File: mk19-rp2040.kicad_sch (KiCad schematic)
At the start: 145 parts, among them J1 USB_C_Receptacle_USB2.0, J10 Conn_01x02, J11 Conn_01x03_Socket, J12 USB_C_Receptacle_USB2.0, J13 USB_C_Receptacle_USB2.0, J2 Conn_01x03_Socket, J3 Conn_01x02_Socket, J4 Conn_01x06_Socket, J5 Conn_01x02, J7 Conn_01x02_Socket, J8 Conn_01x02_Socket, J9 Conn_01x02_Socket, T1 Conn_01x01_Socket, T10 Conn_01x01_Socket, T11 Conn_01x01_Socket, T12 Conn_01x01_Socket, T13 Conn_01x01_Socket, T14 Conn_01x01_Socket, T15 Conn_01x01_Socket, T2 Conn_01x01_Socket, T3 Conn_01x01_Socket, T5 Conn_01x01_Socket, T6 Conn_01x01_Socket, T7 Conn_01x01_Socket, T9 Conn_01x01_Socket, U1 RP2040, U10 1N4148W_C81598, U11 1N4148W_C81598, U12 1N4148W_C81598, U13 1N4148W_C81598, U14 1N4148W_C81598, U15 1N4148W_C81598, U16 W25Q128JVSIQTR, U3 XC6210B332MR-G, U6 8_01A0_008200, U7 8_01A0_008200, U9 1N4148W_C81598, Y1 Crystal_GND24

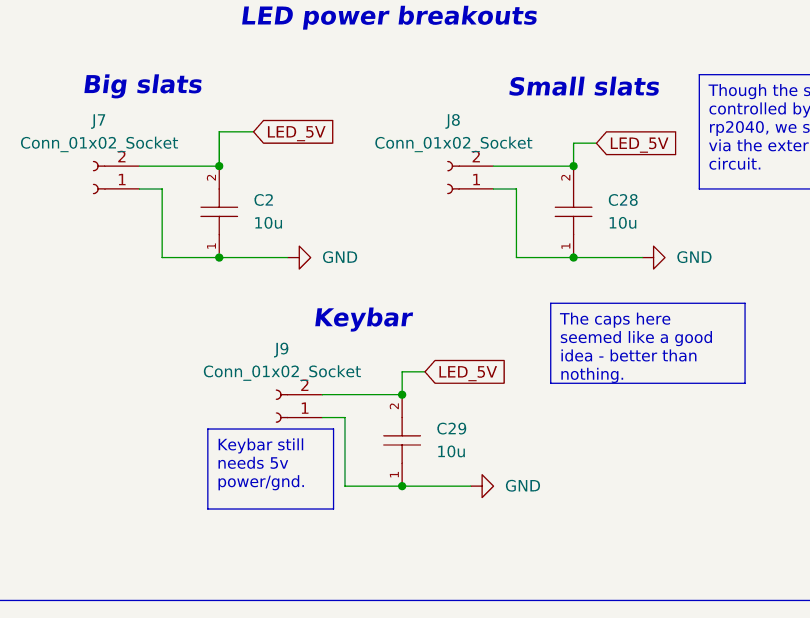
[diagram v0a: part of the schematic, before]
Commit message: removing the other 10u caps and relocating the power in plug
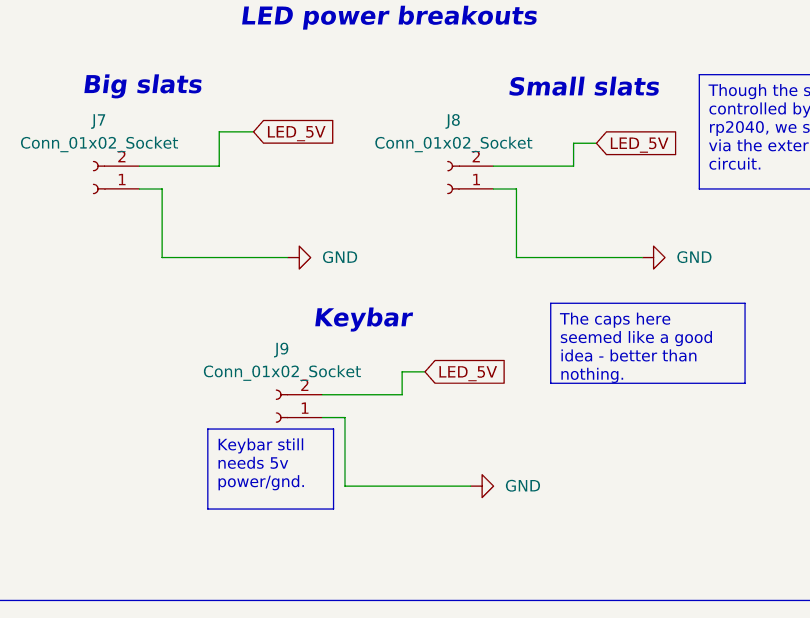
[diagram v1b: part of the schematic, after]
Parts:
- removed C2, C28, C29: 10u, ct-kicad:C0805, symbol ct-kicad:GRM21BR61H106KE43L

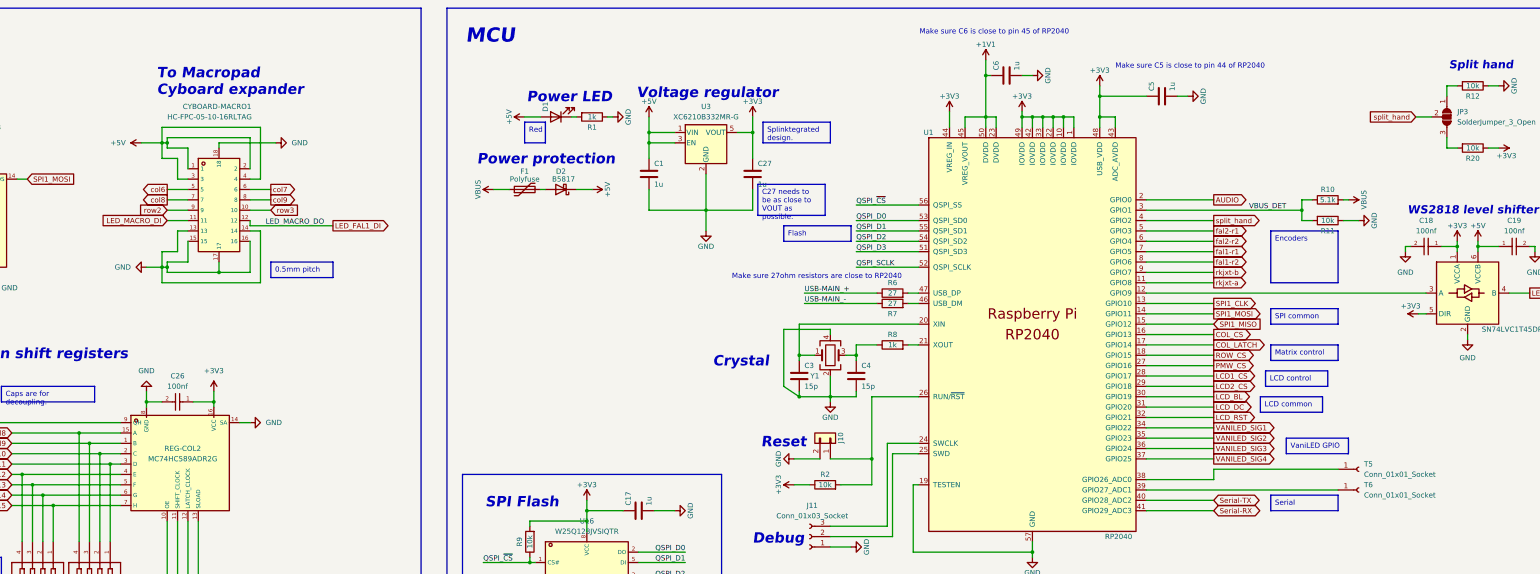
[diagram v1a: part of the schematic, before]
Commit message: replaced the macro connector with a more solid-looking part, more rework
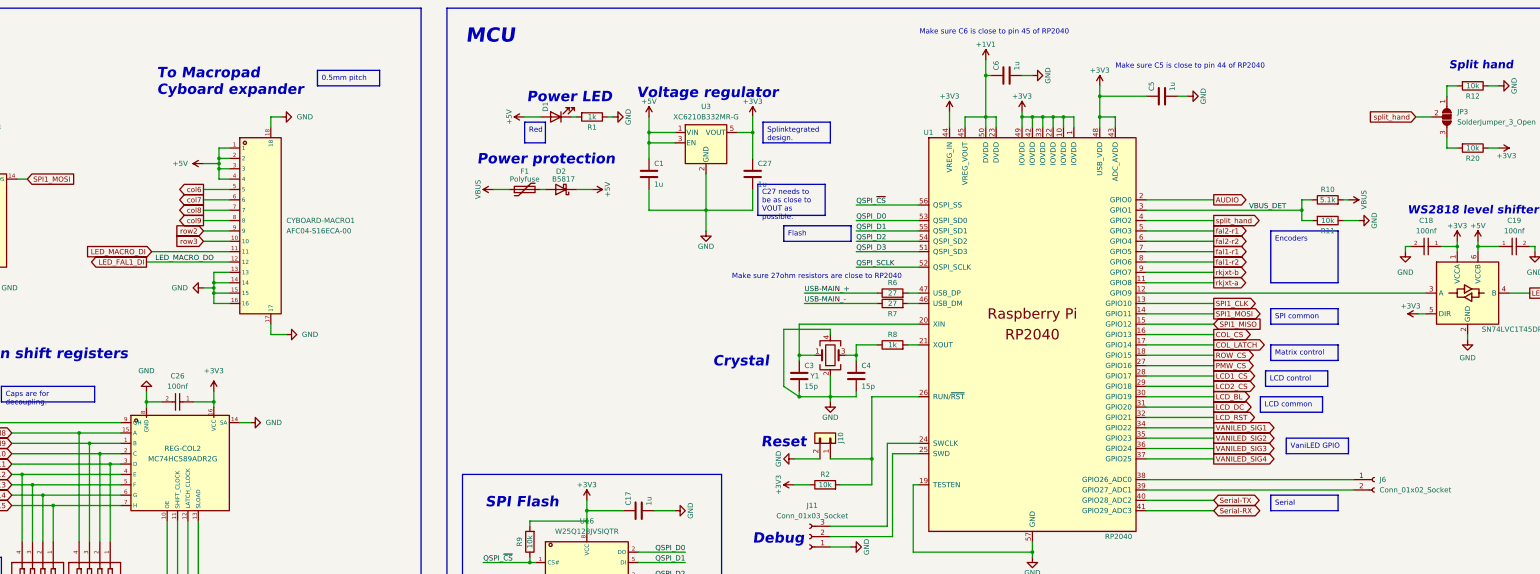
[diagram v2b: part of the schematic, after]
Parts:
- removed CYBOARD-MACRO1: HC-FPC-05-10-16RLTAG, ct-kicad:FPC-SMD_16P-P0.50_HCTL_HC-FPC-05-10-16RLTAG, symbol ct-kicad:0_5K-A-16PBF
- removed T5, T6: Conn_01x01_Socket, Connector_Pin:Pin_D1.0mm_L10.0mm, symbol Connector:Conn_01x01_Socket
- added CYBOARD-MACRO1: AFC04-S16ECA-00, ct-kicad:FPC-SMD_AFC04-S16ECA-00, symbol ct-kicad:AFC04-S16ECA-00
- added J6: Conn_01x02_Socket, Connector_JST:JST_XH_S2B-XH-A_1x02_P2.50mm_Horizontal, symbol Connector:Conn_01x02_Socket
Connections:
- net +5V: now also CYBOARD-MACRO1.1, CYBOARD-MACRO1.2, CYBOARD-MACRO1.3, CYBOARD-MACRO1.4
- net GND: now also CYBOARD-MACRO1.13, CYBOARD-MACRO1.14, CYBOARD-MACRO1.15, CYBOARD-MACRO1.16, CYBOARD-MACRO1.17, CYBOARD-MACRO1.18
- net LED_FAL1_DI: now also CYBOARD-MACRO1.12
- net LED_MACRO_DI: now also CYBOARD-MACRO1.11
- net col6: now also CYBOARD-MACRO1.5
- net col7: now also CYBOARD-MACRO1.6
- net col8: now also CYBOARD-MACRO1.7
- net col9: now also CYBOARD-MACRO1.8
- net row2: now also CYBOARD-MACRO1.9
- net row3: now also CYBOARD-MACRO1.10
- net at U1.38 (GPIO26_ADC0): now also J6.1 (Pin_1)
- net at U1.39 (GPIO27_ADC1): now also J6.2 (Pin_2)

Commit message: fixing silkscreen, changing out polyfuses to larger, improving trace routing
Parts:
- removed F1: Polyfuse, Fuse:Fuse_0603_1608Metric, symbol Device:Polyfuse
- added F1: Polyfuse, ct-kicad:F1206, symbol ct-kicad:RF1989-000
- F2: footprint Fuse:Fuse_0603_1608Metric -> ct-kicad:F1206; symbol Device:Polyfuse -> ct-kicad:RF1989-000; LCSC C69679 -> C2892425
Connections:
- net +5V: no longer VANILED1.2 (Pin_2)
- net VBUS: now also F1.1
- net at JP1.2 (C), JP4.2 (C): now also VANILED1.2 (Pin_2)
- net at D2.2 (A): now also F1.2
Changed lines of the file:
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@@
 	)
 	(junction
+		(at 152.4 414.02)
+		(diameter 0)
+		(color 0 0 0 0)
+	)
+	(junction
 		(at 168.91 129.54)
 		(diameter 0)
@@
 	(wire
 		(pts
-			(xy 339.09 62.23) (xy 340.36 62.23)
-		)
-		(stroke
-			(width 0)
-			(type default)
-		)
-	)
-	(wire
-		(pts
 			(xy 571.5 52.07) (xy 574.04 52.07)
 		)
@@
 	(wire
 		(pts
+			(xy 152.4 414.02) (xy 152.4 425.45)
+		)
+		(stroke
+			(width 0)
+			(type default)
+		)
+	)
+	(wire
+		(pts
 			(xy 143.51 129.54) (xy 168.91 129.54)
 		)
@@
 	(wire
 		(pts
-			(xy 173.99 419.1) (xy 175.26 419.1)
-		)
-		(stroke
-			(width 0)
-			(type default)
-		)
-	)
-	(wire
-		(pts
 			(xy 233.68 265.43) (xy 243.84 265.43)
 		)
@@
 	(wire
 		(pts
-			(xy 152.4 412.75) (xy 152.4 425.45)
+			(xy 152.4 412.75) (xy 152.4 414.02)
 		)
 		(stroke
@@
 	(wire
 		(pts
-			(xy 171.45 375.92) (xy 175.26 375.92)
+			(xy 171.45 375.92) (xy 189.23 375.92)
 		)
 		(stroke
@@
 	(wire
 		(pts
+			(xy 189.23 375.92) (xy 189.23 414.02)
+		)
+		(stroke
+			(width 0)
+			(type default)
+		)
+	)
+	(wire
+		(pts
 			(xy 487.68 138.43) (xy 504.19 138.43)
 		)
@@
 	(wire
 		(pts
+			(xy 173.99 419.1) (xy 175.26 419.1)
+		)
+		(stroke
+			(width 0)
+			(type default)
+		)
+	)
+	(wire
+		(pts
 			(xy 217.17 137.16) (xy 236.22 137.16)
 		)
@@
 	(wire
 		(pts
-			(xy 160.02 419.1) (xy 166.37 419.1)
+			(xy 160.02 419.1) (xy 163.83 419.1)
 		)
 		(stroke
@@
 	(wire
 		(pts
+			(xy 327.66 62.23) (xy 328.93 62.23)
+		)
+		(stroke
+			(width 0)
+			(type default)
+		)
+	)
+	(wire
+		(pts
 			(xy 222.25 275.59) (xy 231.14 275.59)
 		)
@@
 	(wire
 		(pts
+			(xy 339.09 62.23) (xy 340.36 62.23)
+		)
+		(stroke
+			(width 0)
+			(type default)
+		)
+	)
+	(wire
+		(pts
 			(xy 487.68 110.49) (xy 504.19 110.49)
 		)
@@
 	(wire
 		(pts
+			(xy 189.23 414.02) (xy 152.4 414.02)
+		)
+		(stroke
+			(width 0)
+			(type default)
+		)
+	)
+	(wire
+		(pts
 			(xy 335.28 44.45) (xy 339.09 44.45)
 		)
@@
 	(wire
 		(pts
-			(xy 327.66 62.23) (xy 331.47 62.23)
-		)
-		(stroke
-			(width 0)
-			(type default)
-		)
-	)
-	(wire
-		(pts
 			(xy 535.94 69.85) (xy 539.75 69.85)
 		)
@@
 	)
 	(symbol
-		(lib_id "Device:Polyfuse")
-		(at 335.28 62.23 90)
+		(lib_id "Device:FerriteBead_Small")
+		(at 368.3 322.58 270)
 		(unit 1)
 		(exclude_from_sim no)
@@
 		(on_board yes)
 		(dnp no)
-		(property "Reference" "F1"
-			(at 335.28 57.785 90)
+		(property "Reference" "FB2"
+			(at 363.22 325.12 90)
 			(effects
 				(font
 					(size 1.27 1.27)
 				)
+				(justify left)
 			)
 		)
-		(property "Value" "Polyfuse"
-			(at 335.28 59.69 90)
+		(property "Value" "FerriteBead_Small"
+			(at 367.0682 325.12 0)
 			(effects
 				(font
 					(size 1.27 1.27)
 				)
+				(justify left)
+				(hide yes)
 			)
 		)
-		(property "Footprint" "Fuse:Fuse_0603_1608Metric"
-			(at 340.36 60.96 0)
+		(property "Footprint" "Inductor_SMD:L_0603_1608Metric"
+			(at 368.3 320.802 90)
 			(effects
 				(font
 					(size 1.27 1.27)
 				)
-				(justify left)
 				(hide yes)
 			)
 		)
 		(property "Datasheet" "~"
-			(at 335.28 62.23 0)
+			(at 368.3 322.58 0)
 			(effects
 				(font
@@
 		)
 		(property "Description" ""
-			(at 335.28 62.23 0)
+			(at 368.3 322.58 0)
 			(effects
 				(font
@@
 			)
 		)
-		(property "LCSC" "C69679"
-			(at 335.28 62.23 0)
+		(property "LCSC" "C98288"
+			(at 368.3 322.58 0)
 			(effects
 				(font
@@
 			(project "mk19-rp2040"
 				(path "/7353e96a-343a-4876-b497-b1d205a14d97"
-					(reference "F1")
+					(reference "FB2")
 					(unit 1)
 				)
@@
 	)
 	(symbol
-		(lib_id "Device:FerriteBead_Small")
-		(at 368.3 322.58 270)
+		(lib_id "ct-kicad:RF1989-000")
+		(at 334.01 62.23 0)
 		(unit 1)
 		(exclude_from_sim no)
@@
 		(on_board yes)
 		(dnp no)
-		(property "Reference" "FB2"
-			(at 363.22 325.12 90)
+		(property "Reference" "F1"
+			(at 338.455 62.23 90)
 			(effects
 				(font
 					(size 1.27 1.27)
 				)
-				(justify left)
 			)
 		)
-		(property "Value" "FerriteBead_Small"
-			(at 367.0682 325.12 0)
+		(property "Value" "Polyfuse"
+			(at 336.55 62.23 90)
 			(effects
 				(font
 					(size 1.27 1.27)
 				)
-				(justify left)
-				(hide yes)
 			)
 		)
-		(property "Footprint" "Inductor_SMD:L_0603_1608Metric"
-			(at 368.3 320.802 90)
+		(property "Footprint" "ct-kicad:F1206"
+			(at 334.01 72.39 0)
 			(effects
 				(font
 					(size 1.27 1.27)
+					(italic yes)
 				)
 				(hide yes)
 			)
 		)
-		(property "Datasheet" "~"
-			(at 368.3 322.58 0)
+		(property "Datasheet" "https://atta.szlcsc.com/upload/public/pdf/source/20200518/C553934_4CFF0660EAE88BF7A646763F248900C5.pdf"
+			(at 331.724 62.103 0)
 			(effects
 				(font
 					(size 1.27 1.27)
 				)
+				(justify left)
 				(hide yes)
 			)
 		)
 		(property "Description" ""
-			(at 368.3 322.58 0)
+			(at 334.01 62.23 0)
 			(effects
 				(font
@@
 			)
 		)
-		(property "LCSC" "C98288"
-			(at 368.3 322.58 0)
+		(property "LCSC" "C2892425"
+			(at 334.01 62.23 0)
 			(effects
 				(font
@@
 			(project "mk19-rp2040"
 				(path "/7353e96a-343a-4876-b497-b1d205a14d97"
-					(reference "FB2")
+					(reference "F1")
 					(unit 1)
 				)
@@
 	)
 	(symbol
-		(lib_id "Device:Polyfuse")
-		(at 170.18 419.1 90)
+		(lib_id "ct-kicad:RF1989-000")
+		(at 168.91 419.1 0)
 		(unit 1)
 		(exclude_from_sim no)
@@
 		(dnp no)
 		(property "Reference" "F2"
-			(at 170.18 414.655 90)
+			(at 173.355 419.1 90)
 			(effects
 				(font
@@
 		)
 		(property "Value" "Polyfuse"
-			(at 170.18 416.56 90)
+			(at 171.45 419.1 90)
 			(effects
 				(font
@@
 			)
 		)
-		(property "Footprint" "Fuse:Fuse_0603_1608Metric"
-			(at 175.26 417.83 0)
+		(property "Footprint" "ct-kicad:F1206"
+			(at 168.91 429.26 0)
 			(effects
 				(font
 					(size 1.27 1.27)
+					(italic yes)
 				)
-				(justify left)
 				(hide yes)
 			)
 		)
-		(property "Datasheet" "~"
-			(at 170.18 419.1 0)
+		(property "Datasheet" "https://atta.szlcsc.com/upload/public/pdf/source/20200518/C553934_4CFF0660EAE88BF7A646763F248900C5.pdf"
+			(at 166.624 418.973 0)
 			(effects
 				(font
 					(size 1.27 1.27)
 				)
+				(justify left)
 				(hide yes)
 			)
 		)
 		(property "Description" ""
-			(at 170.18 419.1 0)
+			(at 168.91 419.1 0)
 			(effects
 				(font
@@
 			)
 		)
-		(property "LCSC" "C69679"
-			(at 170.18 419.1 0)
+		(property "LCSC" "C2892425"
+			(at 168.91 419.1 0)
 			(effects
 				(font
@@
 					(unit 1)
 				)
-			)
-		)
-	)
-	(symbol
-		(lib_name "+5V_1")
-		(lib_id "power:+5V")
-		(at 175.26 375.92 270)
-		(unit 1)
-		(exclude_from_sim no)
-		(in_bom yes)
-		(on_board yes)
-		(dnp no)
-		(fields_autoplaced yes)
-		(property "Reference" "#PWR036"
-			(at 171.45 375.92 0)
-			(effects
-				(font
-					(size 1.27 1.27)
-				)
-				(hide yes)
-			)
-		)
-		(property "Value" "+5V"
-			(at 179.07 375.9199 90)
-			(effects
-				(font
-					(size 1.27 1.27)
-				)
-				(justify left)
-			)
-		)
-		(property "Footprint" ""
-			(at 175.26 375.92 0)
-			(effects
-				(font
-					(size 1.27 1.27)
-				)
-				(hide yes)
-			)
-		)
-		(property "Datasheet" ""
-			(at 175.26 375.92 0)
-			(effects
-				(font
-					(size 1.27 1.27)
-				)
-				(hide yes)
-			)
-		)
-		(property "Description" "Power symbol creates a global label with name \"+5V\""
-			(at 175.26 375.92 0)
-			(effects
-				(font
-					(size 1.27 1.27)
-				)
-				(hide yes)
-			)
-		)
-		(pin "1"
-		)
-		(instances
-			(project "mk19-rp2040"
-				(path "/7353e96a-343a-4876-b497-b1d205a14d97"
-					(reference "#PWR036")
-					(unit 1)
-				)

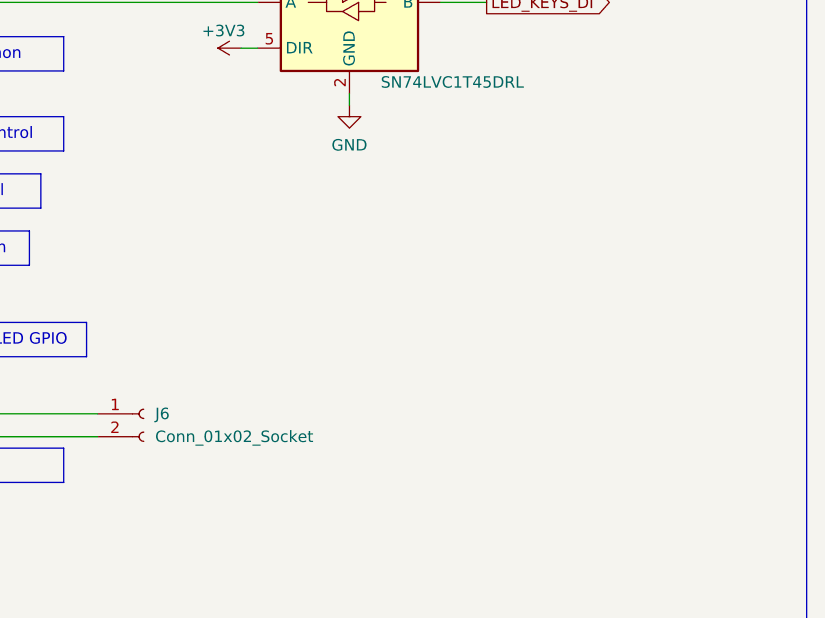
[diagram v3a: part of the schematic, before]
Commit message: adding the pull up-down for spi miso and sck, with solder jumpers
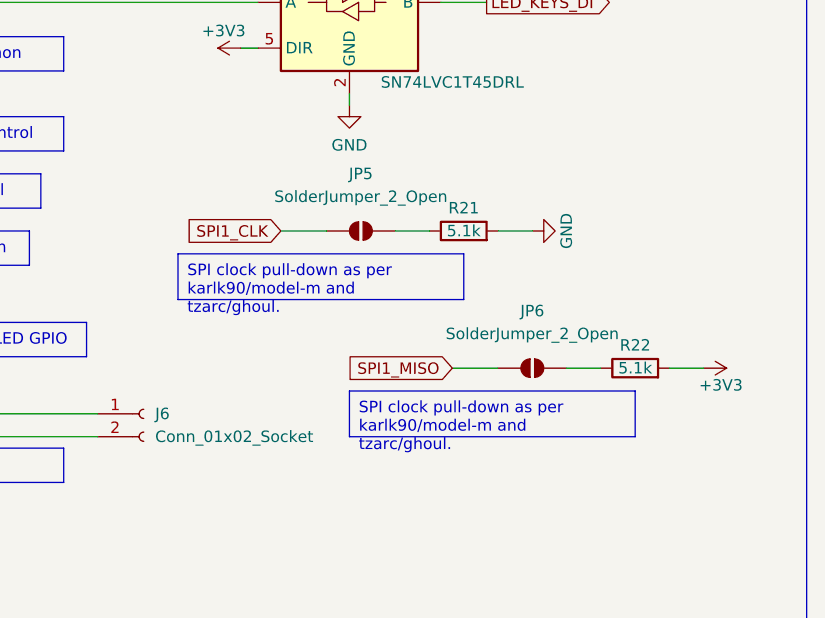
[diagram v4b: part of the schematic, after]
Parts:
- added JP5, JP6: SolderJumper_2_Open, Jumper:SolderJumper-2_P1.3mm_Open_RoundedPad1.0x1.5mm, symbol Jumper:SolderJumper_2_Open
- added R21, R22: 5.1k, ct-kicad:R0402, symbol Device:R
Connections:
- net +3V3: now also R22.2
- net GND: now also R21.2
- net SPI1_CLK: now also JP5.1 (A)
- net SPI1_MISO: now also JP6.1 (A)
- new net: JP5.2 (B), R21.1
- new net: JP6.2 (B), R22.1

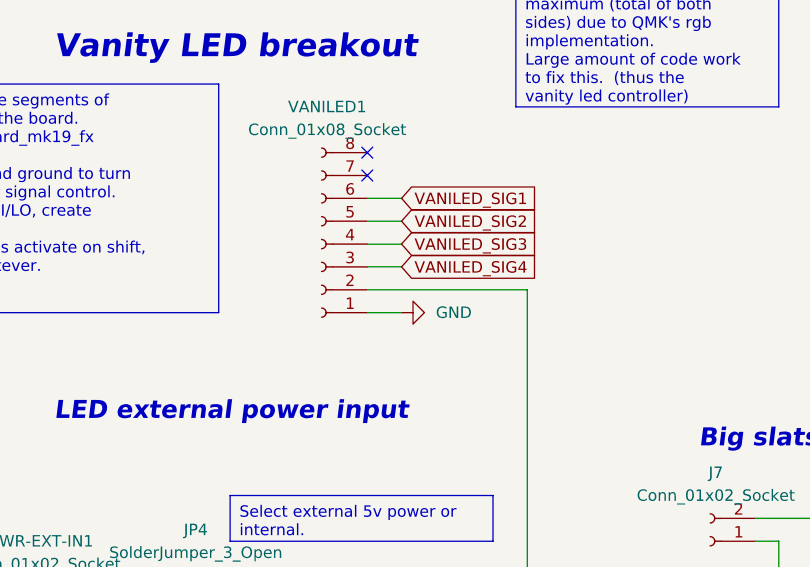
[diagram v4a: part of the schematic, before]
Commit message: moving things around for better physical fitment
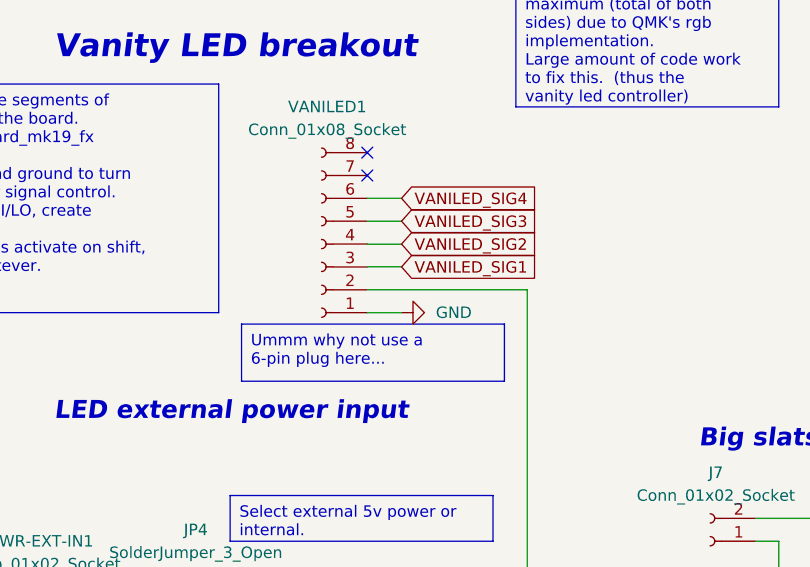
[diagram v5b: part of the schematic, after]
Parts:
- J3: footprint Connector_JST:JST_XH_B2B-XH-A_1x02_P2.50mm_Vertical -> Connector_JST:JST_XH_S2B-XH-A_1x02_P2.50mm_Horizontal
- J7, J8, J9: footprint Connector_JST:JST_XH_S2B-XH-A_1x02_P2.50mm_Horizontal -> Connector_JST:JST_XH_B2B-XH-A_1x02_P2.50mm_Vertical
- VANILED1: footprint Connector_JST:JST_XH_B8B-XH-A_1x08_P2.50mm_Vertical -> Connector_JST:JST_XH_S8B-XH-A_1x08_P2.50mm_Horizontal
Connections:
- net VANILED_SIG1: now also VANILED1.3 (Pin_3); no longer VANILED1.6 (Pin_6)
- net VANILED_SIG2: now also VANILED1.4 (Pin_4); no longer VANILED1.5 (Pin_5)
- net VANILED_SIG3: now also VANILED1.5 (Pin_5); no longer VANILED1.4 (Pin_4)
- net VANILED_SIG4: now also VANILED1.6 (Pin_6); no longer VANILED1.3 (Pin_3)
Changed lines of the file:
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@@
 		)
 	)
+	(text_box "Ummm why not use a 6-pin plug here..."
+		(exclude_from_sim no)
+		(at 157.48 379.73 0)
+		(size 29.21 6.35)
+		(stroke
+			(width 0)
+			(type default)
+		)
+		(fill
+			(type none)
+		)
+		(effects
+			(font
+				(face "Futura")
+				(size 1.27 1.27)
+			)
+			(justify left top)
+		)
+	)
 	(text_box "74HC595 notes\n- When we spi_start(ROW_CS), ROW_CS goes LOW - StorageClock is primed\n- spi_transmit(message) - data is staged!\n- spi_stop(ROW_CS), ROW_CS goes HIGH - StorageClock rises, triggering Latch\n- on Latch, the data is moved to prod! and pins go live with your bits."
 		(exclude_from_sim no)
@@
 		)
 	)
-	(global_label "VANILED_SIG4"
+	(global_label "VANILED_SIG1"
 		(shape input)
 		(at 175.26 373.38 0)
@@
 		)
 	)
-	(global_label "VANILED_SIG3"
+	(global_label "VANILED_SIG2"
 		(shape input)
 		(at 175.26 370.84 0)
@@
 		)
 	)
-	(global_label "VANILED_SIG1"
+	(global_label "VANILED_SIG4"
 		(shape input)
 		(at 175.26 365.76 0)
@@
 		)
 	)
-	(global_label "VANILED_SIG2"
+	(global_label "VANILED_SIG3"
 		(shape input)
 		(at 175.26 368.3 0)
@@
 			)
 		)
-		(property "Footprint" "Connector_JST:JST_XH_S2B-XH-A_1x02_P2.50mm_Horizontal"
+		(property "Footprint" "Connector_JST:JST_XH_B2B-XH-A_1x02_P2.50mm_Vertical"
 			(at 229.87 429.26 0)
 			(effects
@@
 			)
 		)
-		(property "Footprint" "Connector_JST:JST_XH_S2B-XH-A_1x02_P2.50mm_Horizontal"
+		(property "Footprint" "Connector_JST:JST_XH_B2B-XH-A_1x02_P2.50mm_Vertical"
 			(at 209.55 403.86 0)
 			(effects
@@
 			)
 		)
-		(property "Footprint" "Connector_JST:JST_XH_B8B-XH-A_1x08_P2.50mm_Vertical"
+		(property "Footprint" "Connector_JST:JST_XH_S8B-XH-A_1x08_P2.50mm_Horizontal"
 			(at 166.37 370.84 0)
 			(effects
@@
 			)
 		)
-		(property "Footprint" "Connector_JST:JST_XH_B2B-XH-A_1x02_P2.50mm_Vertical"
+		(property "Footprint" "Connector_JST:JST_XH_S2B-XH-A_1x02_P2.50mm_Horizontal"
 			(at 118.11 331.47 0)
 			(effects
@@
 			)
 		)
-		(property "Footprint" "Connector_JST:JST_XH_S2B-XH-A_1x02_P2.50mm_Horizontal"
+		(property "Footprint" "Connector_JST:JST_XH_B2B-XH-A_1x02_P2.50mm_Vertical"
 			(at 248.92 403.86 0)
 			(effects
